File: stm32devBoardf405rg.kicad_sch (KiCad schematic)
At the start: 48 parts, among them J1 Screw_Terminal_01x02, J2 SWD, J3 Conn_01x04, J4 Conn_01x04, J5 USB_B_Micro, Q1 AO3401A, SW1 SW_SPDT, U1 STM32F405RGT6, U2 USBLC6-2SC6, Y1 16MZ

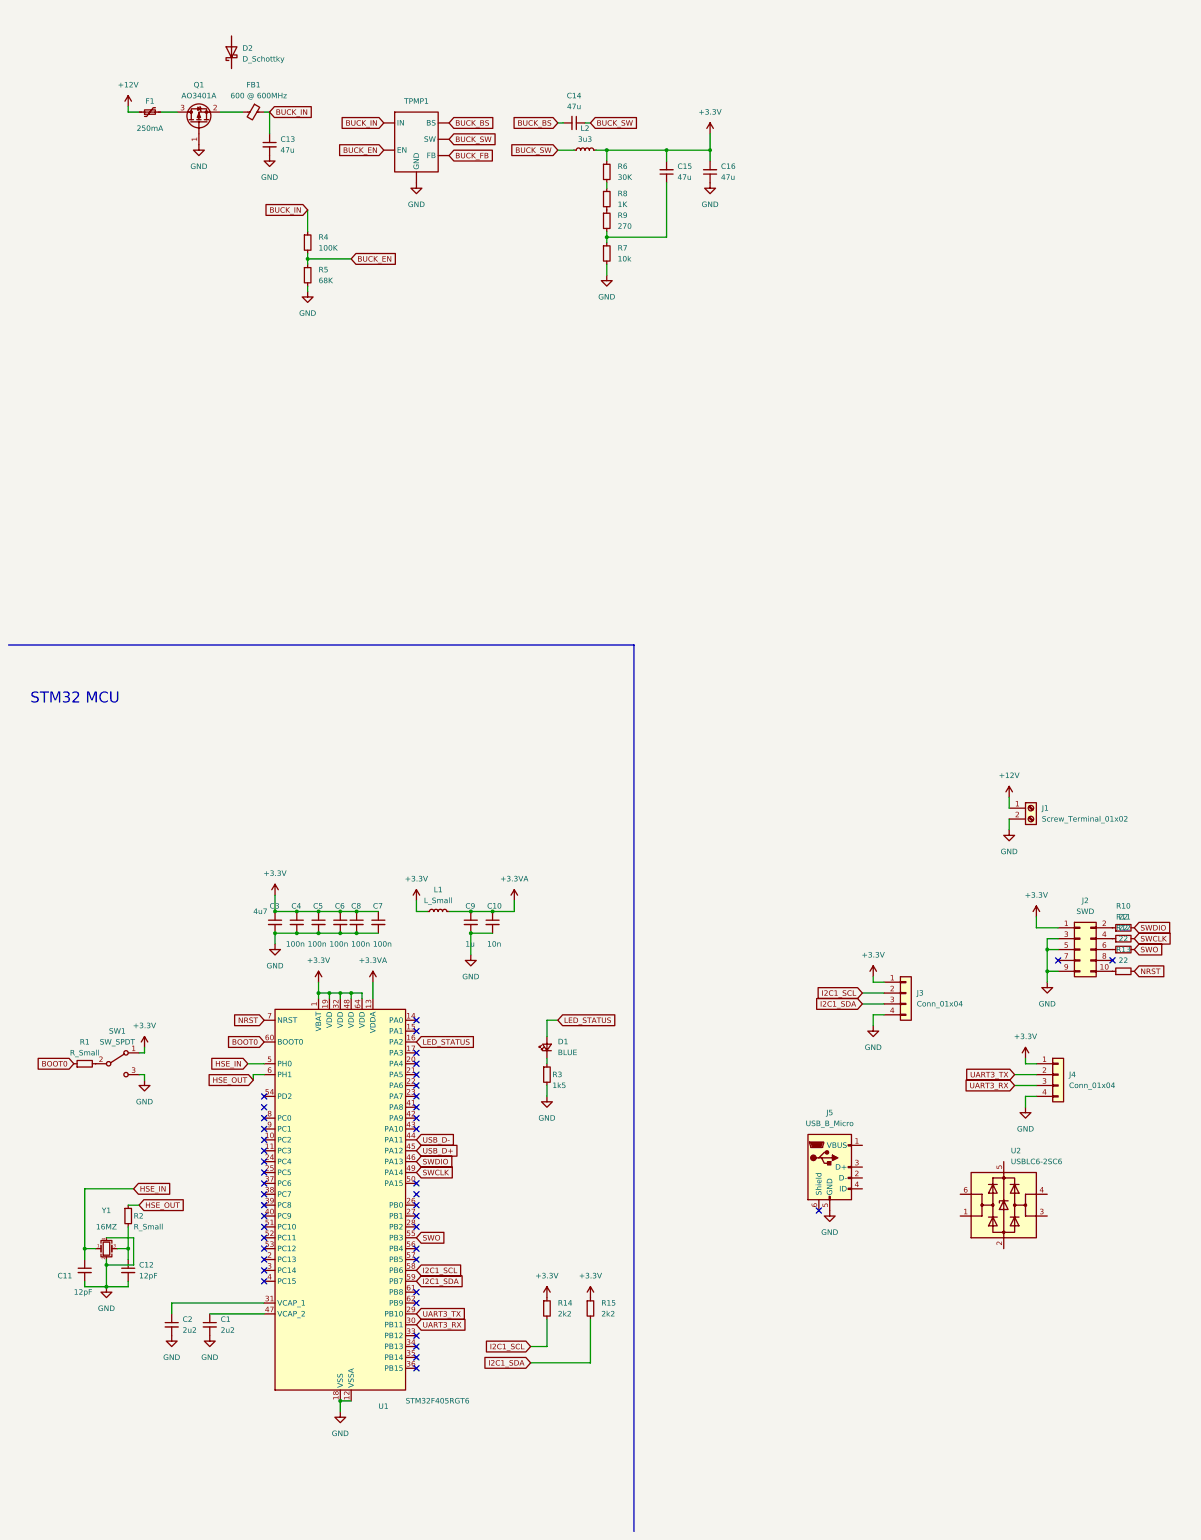
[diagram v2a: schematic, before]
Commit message: USB connector
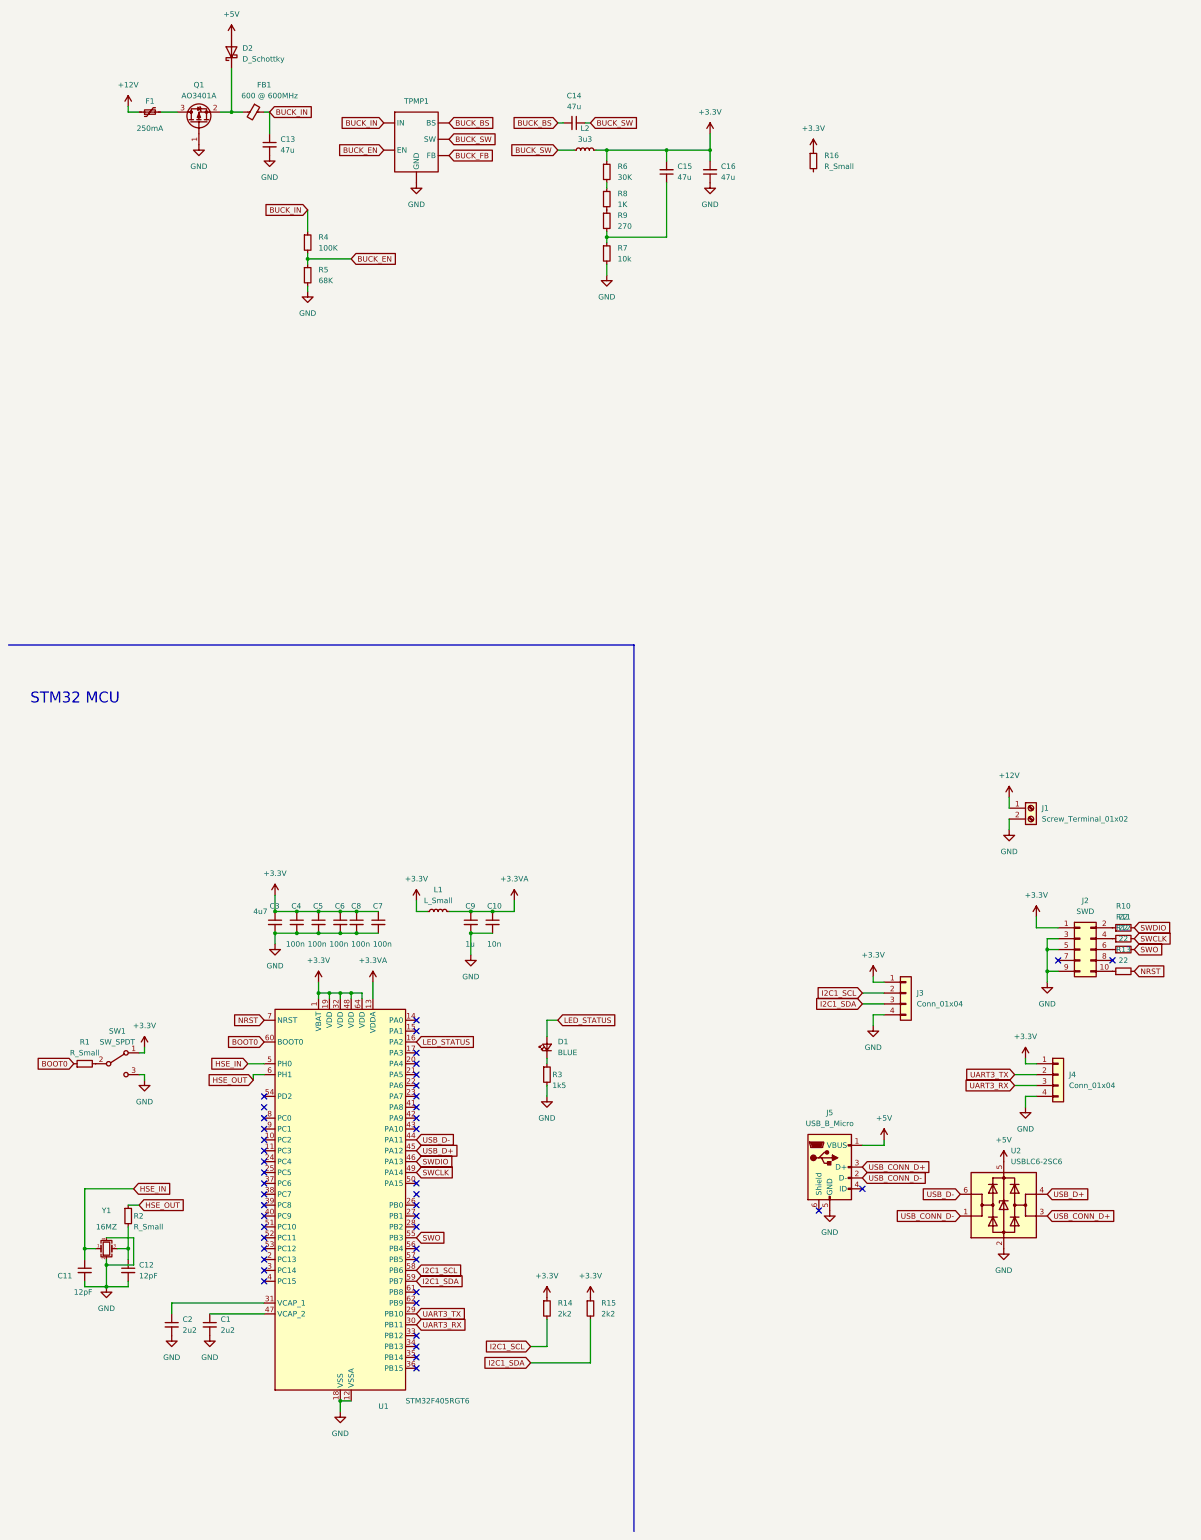
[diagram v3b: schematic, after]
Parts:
- added R16: R_Small, symbol Device:R_Small
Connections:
- net +3.3V: now also R16.1
- net GND: now also U2.2 (GND)
- net USB_D+: now also U2.4 (I/O2)
- net USB_D-: now also U2.6 (I/O1)
- net at FB1.2, Q1.2 (S): now also D2.1 (K)
- net +5V: now reaches J5.1 (VBUS)
- net +5V: now also D2.2 (A), U2.5 (VBUS)
- net USB_CONN_D-: now reaches J5.2 (D-)
- net USB_CONN_D-: now also U2.1 (I/O1)
- net USB_CONN_D+: now reaches J5.3 (D+)
- net USB_CONN_D+: now also U2.3 (I/O2)
- no-connect marks 44 -> 45
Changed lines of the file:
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@@
   (junction (at 93.98 283.21) (diameter 0) (color 0 0 0 0)
+  )
+  (junction (at 66.04 77.47) (diameter 0) (color 0 0 0 0)
   )
   (junction (at 81.28 264.16) (diameter 0) (color 0 0 0 0)
@@
   (no_connect (at 73.66 312.42))
   (no_connect (at 109.22 314.96))
+  (no_connect (at 213.36 328.93))
   (no_connect (at 109.22 304.8))
   (no_connect (at 73.66 342.9))
@@
     (stroke (width 0) (type default))
   )
+  (wire (pts (xy 218.44 317.5) (xy 218.44 318.77))
+    (stroke (width 0) (type default))
+  )
   (wire (pts (xy 251.46 307.34) (xy 251.46 309.88))
     (stroke (width 0) (type default))
   )
+  (wire (pts (xy 66.04 77.47) (xy 68.58 77.47))
+    (stroke (width 0) (type default))
+  )
   (wire (pts (xy 213.36 285.75) (xy 218.44 285.75))
     (stroke (width 0) (type default))
@@
     (stroke (width 0) (type default))
   )
+  (wire (pts (xy 218.44 318.77) (xy 213.36 318.77))
+    (stroke (width 0) (type default))
+  )
   (wire (pts (xy 45.72 297.18) (xy 44.45 297.18))
     (stroke (width 0) (type default))
@@
     (stroke (width 0) (type default))
   )
-  (wire (pts (xy 63.5 77.47) (xy 68.58 77.47))
+  (wire (pts (xy 63.5 77.47) (xy 66.04 77.47))
     (stroke (width 0) (type default))
   )
@@
   )
   (wire (pts (xy 39.37 342.9) (xy 41.91 342.9))
+    (stroke (width 0) (type default))
+  )
+  (wire (pts (xy 66.04 67.31) (xy 66.04 77.47))
     (stroke (width 0) (type default))
   )
@@
     )
   )
+  (global_label "USB_D+" (shape input) (at 256.54 330.2 0) (fields_autoplaced)
+    (effects (font (size 1.27 1.27)) (justify left))
+    (property "Intersheetrefs" "${INTERSHEET_REFS}" (at 267.1452 330.2 0)
+      (effects (font (size 1.27 1.27)) (justify left) hide)
+    )
+  )
   (global_label "UART3_RX" (shape input) (at 248.92 304.8 180) (fields_autoplaced)
     (effects (font (size 1.27 1.27)) (justify right))
@@
     )
   )
+  (global_label "USB_CONN_D-" (shape input) (at 213.36 326.39 0) (fields_autoplaced)
+    (effects (font (size 1.27 1.27)) (justify left))
+    (property "Intersheetrefs" "${INTERSHEET_REFS}" (at 230.1943 326.39 0)
+      (effects (font (size 1.27 1.27)) (justify left) hide)
+    )
+  )
   (global_label "HSE_IN" (shape input) (at 69.85 299.72 180) (fields_autoplaced)
     (effects (font (size 1.27 1.27)) (justify right))
@@
     )
   )
+  (global_label "USB_D-" (shape input) (at 236.22 330.2 180) (fields_autoplaced)
+    (effects (font (size 1.27 1.27)) (justify right))
+    (property "Intersheetrefs" "${INTERSHEET_REFS}" (at 225.6148 330.2 0)
+      (effects (font (size 1.27 1.27)) (justify right) hide)
+    )
+  )
   (global_label "HSE_IN" (shape input) (at 43.18 328.93 0) (fields_autoplaced)
     (effects (font (size 1.27 1.27)) (justify left))
@@
     )
   )
+  (global_label "USB_CONN_D+" (shape input) (at 256.54 335.28 0) (fields_autoplaced)
+    (effects (font (size 1.27 1.27)) (justify left))
+    (property "Intersheetrefs" "${INTERSHEET_REFS}" (at 273.3743 335.28 0)
+      (effects (font (size 1.27 1.27)) (justify left) hide)
+    )
+  )
   (global_label "NRST" (shape input) (at 73.66 289.56 180) (fields_autoplaced)
     (effects (font (size 1.27 1.27)) (justify right))
@@
     )
   )
+  (global_label "USB_CONN_D-" (shape input) (at 236.22 335.28 180) (fields_autoplaced)
+    (effects (font (size 1.27 1.27)) (justify right))
+    (property "Intersheetrefs" "${INTERSHEET_REFS}" (at 219.3857 335.28 0)
+      (effects (font (size 1.27 1.27)) (justify right) hide)
+    )
+  )
   (global_label "I2C1_SCL" (shape input) (at 135.89 365.76 180) (fields_autoplaced)
     (effects (font (size 1.27 1.27)) (justify right))
     (property "Intersheetrefs" "${INTERSHEET_REFS}" (at 124.1358 365.76 0)
       (effects (font (size 1.27 1.27)) (justify right) hide)
+    )
+  )
+  (global_label "USB_CONN_D+" (shape input) (at 213.36 323.85 0) (fields_autoplaced)
+    (effects (font (size 1.27 1.27)) (justify left))
+    (property "Intersheetrefs" "${INTERSHEET_REFS}" (at 230.1943 323.85 0)
+      (effects (font (size 1.27 1.27)) (justify left) hide)
     )
   )
@@
   (symbol (lib_id "Device:FerriteBead_Small") (at 71.12 77.47 270) (unit 1)
     (in_bom yes) (on_board yes) (dnp no)
-    (property "Reference" "FB1" (at 71.1581 71.12 90)
-      (effects (font (size 1.27 1.27)))
-    )
-    (property "Value" "600 @ 600MHz" (at 72.39 73.66 90)
+    (property "Reference" "FB1" (at 73.66 71.12 90)
+      (effects (font (size 1.27 1.27)))
+    )
+    (property "Value" "600 @ 600MHz" (at 74.93 73.66 90)
       (effects (font (size 1.27 1.27)))
     )
@@
         (path "/4aafbf02-ca97-4ee6-bb1e-9822d798faa0"
           (reference "#PWR022") (unit 1)
+        )
+      )
+    )
+  )
+  (symbol (lib_id "power:+3.3V") (at 201.93 86.36 0) (unit 1)
+    (in_bom yes) (on_board yes) (dnp no) (fields_autoplaced)
+    (property "Reference" "#PWR038" (at 201.93 90.17 0)
+      (effects (font (size 1.27 1.27)) hide)
+    )
+    (property "Value" "+3.3V" (at 201.93 81.28 0)
+      (effects (font (size 1.27 1.27)))
+    )
+    (property "Footprint" "" (at 201.93 86.36 0)
+      (effects (font (size 1.27 1.27)) hide)
+    )
+    (property "Datasheet" "" (at 201.93 86.36 0)
+      (effects (font (size 1.27 1.27)) hide)
+    )
+    (pin "1")
+    (instances
+      (project "stm32devBoardf405rg"
+        (path "/4aafbf02-ca97-4ee6-bb1e-9822d798faa0"
+          (reference "#PWR038") (unit 1)
         )
       )
@@
     )
   )
+  (symbol (lib_id "power:+5V") (at 246.38 322.58 0) (unit 1)
+    (in_bom yes) (on_board yes) (dnp no) (fields_autoplaced)
+    (property "Reference" "#PWR036" (at 246.38 326.39 0)
+      (effects (font (size 1.27 1.27)) hide)
+    )
+    (property "Value" "+5V" (at 246.38 317.5 0)
+      (effects (font (size 1.27 1.27)))
+    )
+    (property "Footprint" "" (at 246.38 322.58 0)
+      (effects (font (size 1.27 1.27)) hide)
+    )
+    (property "Datasheet" "" (at 246.38 322.58 0)
+      (effects (font (size 1.27 1.27)) hide)
+    )
+    (pin "1")
+    (instances
+      (project "stm32devBoardf405rg"
+        (path "/4aafbf02-ca97-4ee6-bb1e-9822d798faa0"
+          (reference "#PWR036") (unit 1)
+        )
+      )
+    )
+  )
   (symbol (lib_id "power:GND") (at 52.07 363.22 0) (unit 1)
     (in_bom yes) (on_board yes) (dnp no) (fields_autoplaced)
@@
         (path "/4aafbf02-ca97-4ee6-bb1e-9822d798faa0"
           (reference "R14") (unit 1)
+        )
+      )
+    )
+  )
+  (symbol (lib_id "power:+5V") (at 218.44 317.5 0) (unit 1)
+    (in_bom yes) (on_board yes) (dnp no) (fields_autoplaced)
+    (property "Reference" "#PWR035" (at 218.44 321.31 0)
+      (effects (font (size 1.27 1.27)) hide)
+    )
+    (property "Value" "+5V" (at 218.44 312.42 0)
+      (effects (font (size 1.27 1.27)))
+    )
+    (property "Footprint" "" (at 218.44 317.5 0)
+      (effects (font (size 1.27 1.27)) hide)
+    )
+    (property "Datasheet" "" (at 218.44 317.5 0)
+      (effects (font (size 1.27 1.27)) hide)
+    )
+    (pin "1")
+    (instances
+      (project "stm32devBoardf405rg"
+        (path "/4aafbf02-ca97-4ee6-bb1e-9822d798faa0"
+          (reference "#PWR035") (unit 1)
         )
       )
@@
     )
   )
+  (symbol (lib_id "power:GND") (at 246.38 342.9 0) (unit 1)
+    (in_bom yes) (on_board yes) (dnp no) (fields_autoplaced)
+    (property "Reference" "#PWR037" (at 246.38 349.25 0)
+      (effects (font (size 1.27 1.27)) hide)
+    )
+    (property "Value" "GND" (at 246.38 347.98 0)
+      (effects (font (size 1.27 1.27)))
+    )
+    (property "Footprint" "" (at 246.38 342.9 0)
+      (effects (font (size 1.27 1.27)) hide)
+    )
+    (property "Datasheet" "" (at 246.38 342.9 0)
+      (effects (font (size 1.27 1.27)) hide)
+    )
+    (pin "1")
+    (instances
+      (project "stm32devBoardf405rg"
+        (path "/4aafbf02-ca97-4ee6-bb1e-9822d798faa0"
+          (reference "#PWR037") (unit 1)
+        )
+      )
+    )
+  )
   (symbol (lib_id "Device:R_Small") (at 274.32 273.05 90) (unit 1)
     (in_bom yes) (on_board yes) (dnp no) (fields_autoplaced)
@@
         (path "/4aafbf02-ca97-4ee6-bb1e-9822d798faa0"
           (reference "D2") (unit 1)
+        )
+      )
+    )
+  )
+  (symbol (lib_id "power:+5V") (at 66.04 59.69 0) (unit 1)
+    (in_bom yes) (on_board yes) (dnp no) (fields_autoplaced)
+    (property "Reference" "#PWR034" (at 66.04 63.5 0)
+      (effects (font (size 1.27 1.27)) hide)
+    )
+    (property "Value" "+5V" (at 66.04 54.61 0)
+      (effects (font (size 1.27 1.27)))
+    )
+    (property "Footprint" "" (at 66.04 59.69 0)
+      (effects (font (size 1.27 1.27)) hide)
+    )
+    (property "Datasheet" "" (at 66.04 59.69 0)
+      (effects (font (size 1.27 1.27)) hide)
+    )
+    (pin "1")
+    (instances
+      (project "stm32devBoardf405rg"
+        (path "/4aafbf02-ca97-4ee6-bb1e-9822d798faa0"
+          (reference "#PWR034") (unit 1)
         )
       )
@@
         )
       )
+    )
+  )
+  (symbol (lib_id "Device:R_Small") (at 201.93 88.9 0) (unit 1)
+    (in_bom yes) (on_board yes) (dnp no) (fields_autoplaced)
+    (property "Reference" "R16" (at 204.47 87.63 0)
+      (effects (font (size 1.27 1.27)) (justify left))
+    )
+    (property "Value" "R_Small" (at 204.47 90.17 0)
+      (effects (font (size 1.27 1.27)) (justify left))
+    )
+    (property "Footprint" "" (at 201.93 88.9 0)
+      (effects (font (size 1.27 1.27)) hide)
+    )
+    (property "Datasheet" "~" (at 201.93 88.9 0)
+      (effects (font (size 1.27 1.27)) hide)
+    )
+    (pin "1")
+    (pin "2")
+    (instances
+      (project "stm32devBoardf405rg"
+        (path "/4aafbf02-ca97-4ee6-bb1e-9822d798faa0"
+          (reference "R16") (unit 1)
+        )
+      )

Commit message: USB connector II
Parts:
- added D3: LED, symbol Device:LED
- R16: value R_Small -> 1K
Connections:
- net GND: now also D3.1 (K)
- net at R16.2: now also D3.2 (A)
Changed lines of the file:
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@@
+    )
+  )
+  (symbol (lib_id "power:GND") (at 201.93 99.06 0) (unit 1)
+    (in_bom yes) (on_board yes) (dnp no) (fields_autoplaced)
+    (property "Reference" "#PWR039" (at 201.93 105.41 0)
+      (effects (font (size 1.27 1.27)) hide)
+    )
+    (property "Value" "GND" (at 201.93 104.14 0)
+      (effects (font (size 1.27 1.27)))
+    )
+    (property "Footprint" "" (at 201.93 99.06 0)
+      (effects (font (size 1.27 1.27)) hide)
+    )
+    (property "Datasheet" "" (at 201.93 99.06 0)
+      (effects (font (size 1.27 1.27)) hide)
+    )
+    (pin "1")
+    (instances
+      (project "stm32devBoardf405rg"
+        (path "/4aafbf02-ca97-4ee6-bb1e-9822d798faa0"
+          (reference "#PWR039") (unit 1)
+        )
+      )
     )
   )
@@
     )
   )
+  (symbol (lib_id "Device:LED") (at 201.93 95.25 90) (unit 1)
+    (in_bom yes) (on_board yes) (dnp no) (fields_autoplaced)
+    (property "Reference" "D3" (at 205.74 95.5675 90)
+      (effects (font (size 1.27 1.27)) (justify right))
+    )
+    (property "Value" "LED" (at 205.74 98.1075 90)
+      (effects (font (size 1.27 1.27)) (justify right))
+    )
+    (property "Footprint" "" (at 201.93 95.25 0)
+      (effects (font (size 1.27 1.27)) hide)
+    )
+    (property "Datasheet" "~" (at 201.93 95.25 0)
+      (effects (font (size 1.27 1.27)) hide)
+    )
+    (pin "1")
+    (pin "2")
+    (instances
+      (project "stm32devBoardf405rg"
+        (path "/4aafbf02-ca97-4ee6-bb1e-9822d798faa0"
+          (reference "D3") (unit 1)
+        )
+      )
+    )
+  )
   (symbol (lib_id "Device:C_Small") (at 127 266.7 0) (unit 1)
     (in_bom yes) (on_board yes) (dnp no)
@@
       (effects (font (size 1.27 1.27)) (justify left))
     )
-    (property "Value" "R_Small" (at 204.47 90.17 0)
-      (effects (font (size 1.27 1.27)) (justify left))
-    )
+    (property "Value" "1K" (at 204.47 90.17 0)
+      (effects (font (size 1.27 1.27)) (justify left))
+    )

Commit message: added footprint
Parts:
- added H1, H2, H3, H4: MountingHole_Pad, MountingHole:MountingHole_4.3mm_M4_Pad_Via, symbol Mechanical:MountingHole_Pad
- C1, C13, C14, C15, C16, C2, C3: footprint (none) -> Capacitor_SMD:C_0603_1608Metric
- C10, C11, C12, C4, C5, C6, C7, C8, C9: footprint (none) -> Capacitor_SMD:C_0402_1005Metric
- D1: footprint (none) -> LED_SMD:LED_0603_1608Metric
- D2: value D_Schottky -> B5819W; footprint (none) -> Diode_SMD:D_SOD-123
- D3: value LED -> RED; footprint (none) -> LED_SMD:LED_0603_1608Metric
- J1: footprint (none) -> TerminalBlock_Phoenix:TerminalBlock_Phoenix_PT-1,5-2-3.5-H_1x02_P3.50mm_Horizontal
- J2: footprint (none) -> Connector_PinSocket_1.27mm:PinSocket_2x05_P1.27mm_Vertical_SMD
- J3, J4: footprint (none) -> Connector_Molex:Molex_PicoBlade_53048-0410_1x04_P1.25mm_Horizontal
- J5: footprint (none) -> Connector_USB:USB_Micro-B_Amphenol_10103594-0001LF_Horizontal
- L1: value L_Small -> 3u3
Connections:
- net GND: now also H1.1, H2.1, H3.1, H4.1
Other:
- moved on the sheet: C13, C14, C15, C16, D2, D3, F1, FB1, L2, Q1, R16, R4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
